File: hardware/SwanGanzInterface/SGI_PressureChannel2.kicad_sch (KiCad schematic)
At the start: 18 parts, among them J7 Conn_01x04_Pin, U12 INA122D, U13 OPA2350

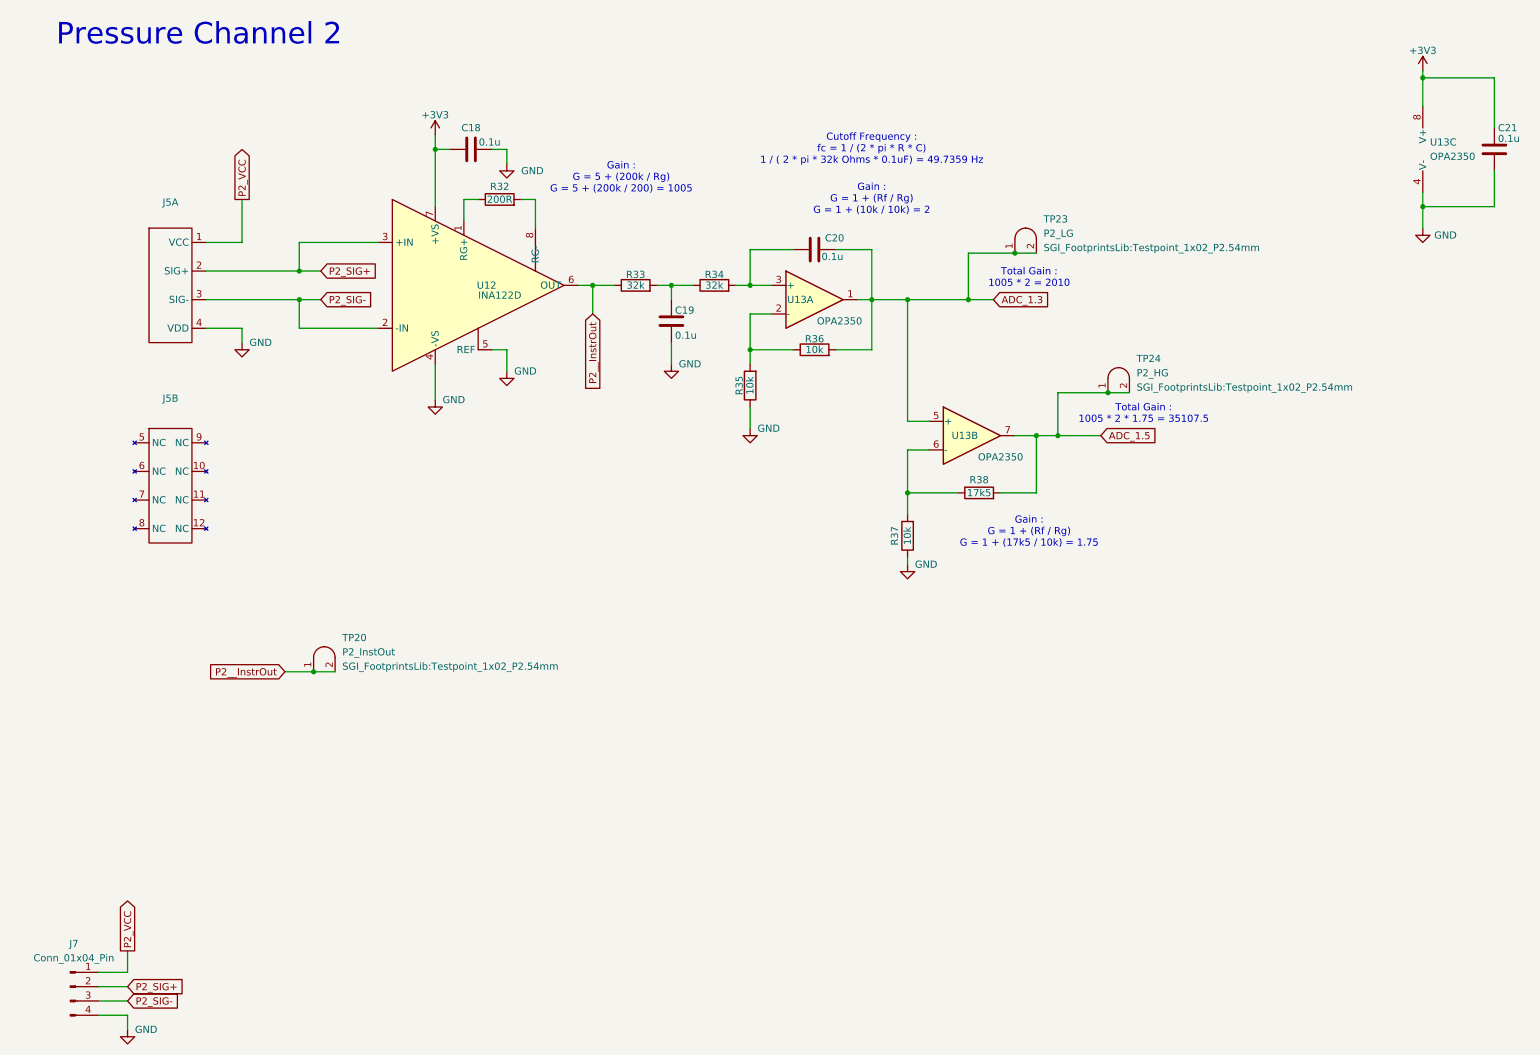
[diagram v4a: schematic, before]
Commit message: Reannotated symbols
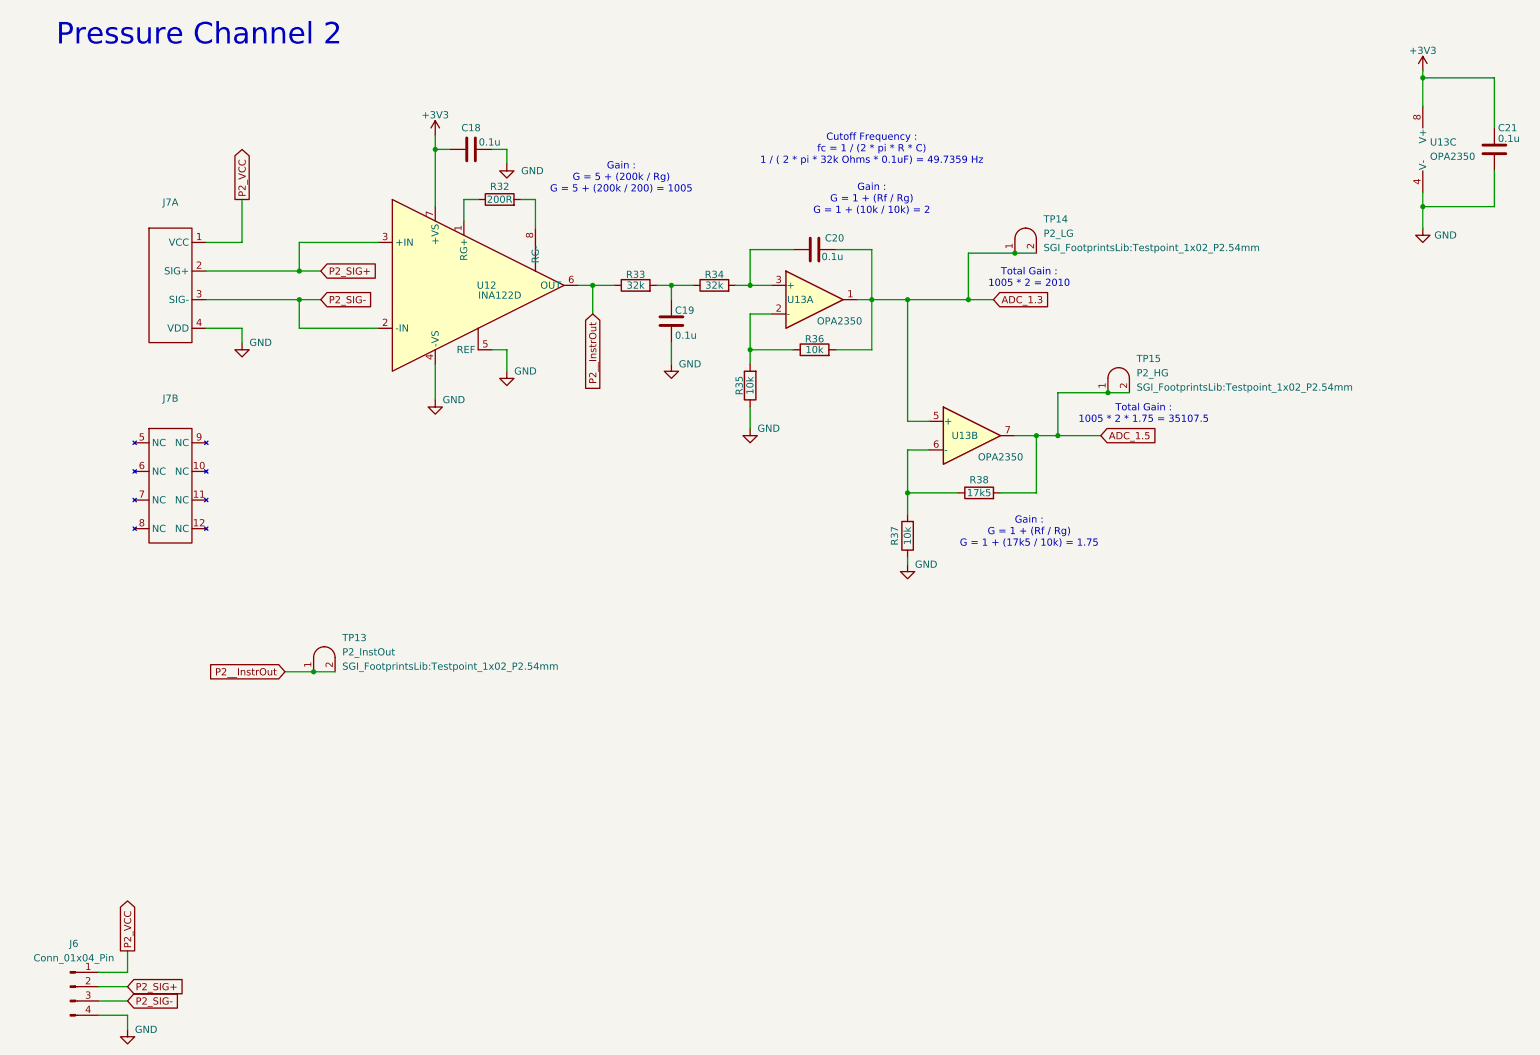
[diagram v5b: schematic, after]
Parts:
- renumbered J7 to J6, J5 to J7, TP20 to TP13, TP23 to TP14, TP24 to TP15
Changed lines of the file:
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@@
 		(on_board yes)
 		(dnp no)
-		(property "Reference" "#PWR070"
+		(property "Reference" "#PWR069"
 			(at 259.08 27.94 0)
 			(effects
@@
 			(project "SwanGanzInterface"
 				(path "/4e9a6e30-f660-472b-9696-bea1f34b4545/5b443651-3bea-4d19-bd25-a234ca65ad96"
-					(reference "#PWR070")
+					(reference "#PWR069")
 					(unit 1)
 				)
@@
 		(on_board yes)
 		(dnp no)
-		(property "Reference" "#PWR073"
+		(property "Reference" "#PWR060"
 			(at 29.21 200.66 0)
 			(effects
@@
 			(project "SwanGanzInterface"
 				(path "/4e9a6e30-f660-472b-9696-bea1f34b4545/5b443651-3bea-4d19-bd25-a234ca65ad96"
-					(reference "#PWR073")
+					(reference "#PWR060")
 					(unit 1)
 				)
@@
 		(dnp no)
 		(fields_autoplaced yes)
-		(property "Reference" "J7"
+		(property "Reference" "J6"
 			(at 19.685 179.07 0)
 			(effects
@@
 			(project "SwanGanzInterface"
 				(path "/4e9a6e30-f660-472b-9696-bea1f34b4545/5b443651-3bea-4d19-bd25-a234ca65ad96"
-					(reference "J7")
+					(reference "J6")
 					(unit 1)
 				)
@@
 		(dnp no)
 		(fields_autoplaced yes)
-		(property "Reference" "J5"
+		(property "Reference" "J7"
 			(at 36.83 47.498 0)
 			(effects
@@
 			(project "SwanGanzInterface"
 				(path "/4e9a6e30-f660-472b-9696-bea1f34b4545/5b443651-3bea-4d19-bd25-a234ca65ad96"
-					(reference "J5")
+					(reference "J7")
 					(unit 1)
 				)
@@
 		(on_board yes)
 		(dnp no)
-		(property "Reference" "#PWR069"
+		(property "Reference" "#PWR068"
 			(at 167.64 118.11 0)
 			(effects
@@
 			(project "SwanGanzInterface"
 				(path "/4e9a6e30-f660-472b-9696-bea1f34b4545/5b443651-3bea-4d19-bd25-a234ca65ad96"
-					(reference "#PWR069")
+					(reference "#PWR068")
 					(unit 1)
 				)
@@
 		(on_board yes)
 		(dnp no)
-		(property "Reference" "#PWR067"
+		(property "Reference" "#PWR066"
 			(at 125.73 82.55 0)
 			(effects
@@
 			(project "SwanGanzInterface"
 				(path "/4e9a6e30-f660-472b-9696-bea1f34b4545/5b443651-3bea-4d19-bd25-a234ca65ad96"
-					(reference "#PWR067")
+					(reference "#PWR066")
 					(unit 1)
 				)
@@
 		(on_board yes)
 		(dnp no)
-		(property "Reference" "#PWR068"
+		(property "Reference" "#PWR067"
 			(at 139.7 93.98 0)
 			(effects
@@
 			(project "SwanGanzInterface"
 				(path "/4e9a6e30-f660-472b-9696-bea1f34b4545/5b443651-3bea-4d19-bd25-a234ca65ad96"
-					(reference "#PWR068")
+					(reference "#PWR067")
 					(unit 1)
 				)
@@
 		(dnp no)
 		(fields_autoplaced yes)
-		(property "Reference" "TP23"
+		(property "Reference" "TP14"
 			(at 191.77 50.4823 0)
 			(effects
@@
 			(project "SwanGanzInterface"
 				(path "/4e9a6e30-f660-472b-9696-bea1f34b4545/5b443651-3bea-4d19-bd25-a234ca65ad96"
-					(reference "TP23")
+					(reference "TP14")
 					(unit 1)
 				)
@@
 		(dnp no)
 		(fields_autoplaced yes)
-		(property "Reference" "TP20"
+		(property "Reference" "TP13"
 			(at 67.31 124.7773 0)
 			(effects
@@
 			(project "SwanGanzInterface"
 				(path "/4e9a6e30-f660-472b-9696-bea1f34b4545/5b443651-3bea-4d19-bd25-a234ca65ad96"
-					(reference "TP20")
+					(reference "TP13")
 					(unit 1)
 				)
@@
 		(dnp no)
 		(fields_autoplaced yes)
-		(property "Reference" "J5"
+		(property "Reference" "J7"
 			(at 36.83 82.296 0)
 			(effects
@@
 			(project "SwanGanzInterface"
 				(path "/4e9a6e30-f660-472b-9696-bea1f34b4545/5b443651-3bea-4d19-bd25-a234ca65ad96"
-					(reference "J5")
+					(reference "J7")
 					(unit 2)
 				)
@@
 		(on_board yes)
 		(dnp no)
-		(property "Reference" "#PWR064"
+		(property "Reference" "#PWR063"
 			(at 83.82 88.9 0)
 			(effects
@@
 			(project "SwanGanzInterface"
 				(path "/4e9a6e30-f660-472b-9696-bea1f34b4545/5b443651-3bea-4d19-bd25-a234ca65ad96"
-					(reference "#PWR064")
+					(reference "#PWR063")
 					(unit 1)
 				)
@@
 		(dnp no)
 		(fields_autoplaced yes)
-		(property "Reference" "TP24"
+		(property "Reference" "TP15"
 			(at 208.28 75.2473 0)
 			(effects
@@
 			(project "SwanGanzInterface"
 				(path "/4e9a6e30-f660-472b-9696-bea1f34b4545/5b443651-3bea-4d19-bd25-a234ca65ad96"
-					(reference "TP24")
+					(reference "TP15")
 					(unit 1)
 				)
@@
 		(dnp no)
 		(fields_autoplaced yes)
-		(property "Reference" "#PWR071"
+		(property "Reference" "#PWR070"
 			(at 259.08 58.42 0)
 			(effects
@@
 			(project "SwanGanzInterface"
 				(path "/4e9a6e30-f660-472b-9696-bea1f34b4545/5b443651-3bea-4d19-bd25-a234ca65ad96"
-					(reference "#PWR071")
+					(reference "#PWR070")
 					(unit 1)
 				)
@@
 		(on_board yes)
 		(dnp no)
-		(property "Reference" "#PWR063"
+		(property "Reference" "#PWR062"
 			(at 83.82 39.37 0)
 			(effects
@@
 			(project "SwanGanzInterface"
 				(path "/4e9a6e30-f660-472b-9696-bea1f34b4545/5b443651-3bea-4d19-bd25-a234ca65ad96"
-					(reference "#PWR063")
+					(reference "#PWR062")
 					(unit 1)
 				)
@@
 		(dnp no)
 		(fields_autoplaced yes)
-		(property "Reference" "#PWR065"
+		(property "Reference" "#PWR064"
 			(at 96.52 46.99 0)
 			(effects
@@
 			(project "SwanGanzInterface"
 				(path "/4e9a6e30-f660-472b-9696-bea1f34b4545/5b443651-3bea-4d19-bd25-a234ca65ad96"
-					(reference "#PWR065")
+					(reference "#PWR064")
 					(unit 1)
 				)
@@
 		(on_board yes)
 		(dnp no)
-		(property "Reference" "#PWR062"
+		(property "Reference" "#PWR061"
 			(at 49.53 78.74 0)
 			(effects
@@
 			(project "SwanGanzInterface"
 				(path "/4e9a6e30-f660-472b-9696-bea1f34b4545/5b443651-3bea-4d19-bd25-a234ca65ad96"
-					(reference "#PWR062")
+					(reference "#PWR061")
 					(unit 1)
 				)
@@
 		(on_board yes)
 		(dnp no)
-		(property "Reference" "#PWR066"
+		(property "Reference" "#PWR065"
 			(at 96.52 83.82 0)
 			(effects
@@
 			(project "SwanGanzInterface"
 				(path "/4e9a6e30-f660-472b-9696-bea1f34b4545/5b443651-3bea-4d19-bd25-a234ca65ad96"
-					(reference "#PWR066")
-					(unit 1)
-				)
+					(reference "#PWR065")
+					(unit 1)
+				)

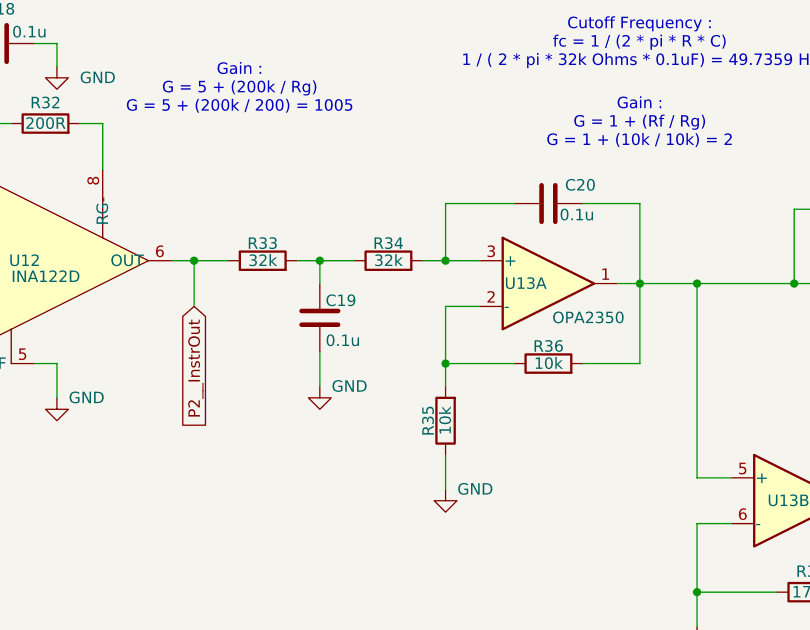
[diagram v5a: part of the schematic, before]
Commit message: Fixed butterworth filters
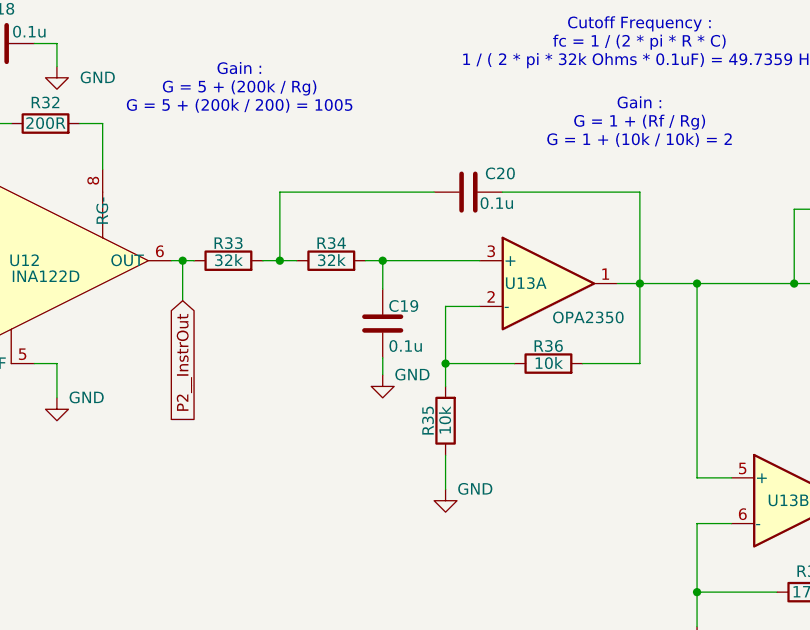
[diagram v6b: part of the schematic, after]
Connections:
- net at R33.2, R34.1: now also C20.1; no longer C19.1
- net at R34.2, U13.3 (+): now also C19.1; no longer C20.1
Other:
- moved on the sheet: C19, C20, R33, R34

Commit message: Implemented Jack's new pressure footprint and added teardrop - new production file
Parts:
- J7: footprint SGI_FootprintsLib:Pressure_Connector -> SGI_FootprintsLib:Pressure_Connector_1.1
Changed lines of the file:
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@@
 			)
 		)
-		(property "Footprint" "SGI_FootprintsLib:Pressure_Connector"
+		(property "Footprint" "SGI_FootprintsLib:Pressure_Connector_1.1"
 			(at 36.83 62.23 0)
 			(effects
@@
 			)
 		)
-		(property "Footprint" "SGI_FootprintsLib:Pressure_Connector"
+		(property "Footprint" "SGI_FootprintsLib:Pressure_Connector_1.1"
 			(at 36.83 97.79 0)
 			(effects

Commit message: Driver Power
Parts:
- renumbered R32 to R31, R33 to R32, R34 to R33, R35 to R34, R36 to R35, R37 to R36, R38 to R37
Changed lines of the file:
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@@
 		(on_board yes)
 		(dnp no)
-		(property "Reference" "#PWR069"
+		(property "Reference" "#PWR068"
 			(at 259.08 27.94 0)
 			(effects
@@
 			(project "SwanGanzInterface"
 				(path "/4e9a6e30-f660-472b-9696-bea1f34b4545/5b443651-3bea-4d19-bd25-a234ca65ad96"
-					(reference "#PWR069")
+					(reference "#PWR068")
 					(unit 1)
 				)
@@
 		(on_board yes)
 		(dnp no)
-		(property "Reference" "#PWR060"
+		(property "Reference" "#PWR059"
 			(at 29.21 200.66 0)
 			(effects
@@
 			(project "SwanGanzInterface"
 				(path "/4e9a6e30-f660-472b-9696-bea1f34b4545/5b443651-3bea-4d19-bd25-a234ca65ad96"
-					(reference "#PWR060")
+					(reference "#PWR059")
 					(unit 1)
 				)
@@
 		(on_board yes)
 		(dnp no)
-		(property "Reference" "#PWR068"
+		(property "Reference" "#PWR067"
 			(at 167.64 118.11 0)
 			(effects
@@
 			(project "SwanGanzInterface"
 				(path "/4e9a6e30-f660-472b-9696-bea1f34b4545/5b443651-3bea-4d19-bd25-a234ca65ad96"
-					(reference "#PWR068")
+					(reference "#PWR067")
 					(unit 1)
 				)
@@
 		(on_board yes)
 		(dnp no)
-		(property "Reference" "R36"
+		(property "Reference" "R35"
 			(at 151.13 71.755 90)
 			(effects
@@
 			(project "SwanGanzInterface"
 				(path "/4e9a6e30-f660-472b-9696-bea1f34b4545/5b443651-3bea-4d19-bd25-a234ca65ad96"
-					(reference "R36")
+					(reference "R35")
 					(unit 1)
 				)
@@
 		(on_board yes)
 		(dnp no)
-		(property "Reference" "R33"
+		(property "Reference" "R32"
 			(at 115.57 60.325 90)
 			(effects
@@
 			(project "SwanGanzInterface"
 				(path "/4e9a6e30-f660-472b-9696-bea1f34b4545/5b443651-3bea-4d19-bd25-a234ca65ad96"
-					(reference "R33")
+					(reference "R32")
 					(unit 1)
 				)
@@
 		(on_board yes)
 		(dnp no)
-		(property "Reference" "#PWR066"
+		(property "Reference" "#PWR065"
 			(at 132.715 81.28 0)
 			(effects
@@
 			(project "SwanGanzInterface"
 				(path "/4e9a6e30-f660-472b-9696-bea1f34b4545/5b443651-3bea-4d19-bd25-a234ca65ad96"
-					(reference "#PWR066")
+					(reference "#PWR065")
 					(unit 1)
 				)
@@
 		(on_board yes)
 		(dnp no)
-		(property "Reference" "#PWR067"
+		(property "Reference" "#PWR066"
 			(at 139.7 93.98 0)
 			(effects
@@
 			(project "SwanGanzInterface"
 				(path "/4e9a6e30-f660-472b-9696-bea1f34b4545/5b443651-3bea-4d19-bd25-a234ca65ad96"
-					(reference "#PWR067")
+					(reference "#PWR066")
 					(unit 1)
 				)
@@
 		(on_board yes)
 		(dnp no)
-		(property "Reference" "R35"
+		(property "Reference" "R34"
 			(at 137.795 80.01 90)
 			(effects
@@
 			(project "SwanGanzInterface"
 				(path "/4e9a6e30-f660-472b-9696-bea1f34b4545/5b443651-3bea-4d19-bd25-a234ca65ad96"
-					(reference "R35")
+					(reference "R34")
 					(unit 1)
 				)
@@
 		(on_board yes)
 		(dnp no)
-		(property "Reference" "R32"
+		(property "Reference" "R31"
 			(at 95.25 44.704 90)
 			(effects
@@
 			(project "SwanGanzInterface"
 				(path "/4e9a6e30-f660-472b-9696-bea1f34b4545/5b443651-3bea-4d19-bd25-a234ca65ad96"
-					(reference "R32")
+					(reference "R31")
 					(unit 1)
 				)
@@
 		(on_board yes)
 		(dnp no)
-		(property "Reference" "#PWR063"
+		(property "Reference" "#PWR062"
 			(at 83.82 88.9 0)
 			(effects
@@
 			(project "SwanGanzInterface"
 				(path "/4e9a6e30-f660-472b-9696-bea1f34b4545/5b443651-3bea-4d19-bd25-a234ca65ad96"
-					(reference "#PWR063")
+					(reference "#PWR062")
 					(unit 1)
 				)
@@
 		(on_board yes)
 		(dnp no)
-		(property "Reference" "R34"
+		(property "Reference" "R33"
 			(at 127 60.325 90)
 			(effects
@@
 			(project "SwanGanzInterface"
 				(path "/4e9a6e30-f660-472b-9696-bea1f34b4545/5b443651-3bea-4d19-bd25-a234ca65ad96"
-					(reference "R34")
+					(reference "R33")
 					(unit 1)
 				)
@@
 		(on_board yes)
 		(dnp no)
-		(property "Reference" "R38"
+		(property "Reference" "R37"
 			(at 180.34 96.774 90)
 			(effects
@@
 			(project "SwanGanzInterface"
 				(path "/4e9a6e30-f660-472b-9696-bea1f34b4545/5b443651-3bea-4d19-bd25-a234ca65ad96"
-					(reference "R38")
+					(reference "R37")
 					(unit 1)
 				)
@@
 		(dnp no)
 		(fields_autoplaced yes)
-		(property "Reference" "#PWR070"
+		(property "Reference" "#PWR069"
 			(at 259.08 58.42 0)
 			(effects
@@
 			(project "SwanGanzInterface"
 				(path "/4e9a6e30-f660-472b-9696-bea1f34b4545/5b443651-3bea-4d19-bd25-a234ca65ad96"
-					(reference "#PWR070")
+					(reference "#PWR069")
 					(unit 1)
 				)
@@
 		(on_board yes)
 		(dnp no)
-		(property "Reference" "#PWR062"
+		(property "Reference" "#PWR061"
 			(at 83.82 39.37 0)
 			(effects
@@
 			(project "SwanGanzInterface"
 				(path "/4e9a6e30-f660-472b-9696-bea1f34b4545/5b443651-3bea-4d19-bd25-a234ca65ad96"
-					(reference "#PWR062")
+					(reference "#PWR061")
 					(unit 1)
 				)
@@
 		(dnp no)
 		(fields_autoplaced yes)
-		(property "Reference" "#PWR064"
+		(property "Reference" "#PWR063"
 			(at 96.52 46.99 0)
 			(effects
@@
 			(project "SwanGanzInterface"
 				(path "/4e9a6e30-f660-472b-9696-bea1f34b4545/5b443651-3bea-4d19-bd25-a234ca65ad96"
-					(reference "#PWR064")
+					(reference "#PWR063")
 					(unit 1)
 				)
@@
 		(on_board yes)
 		(dnp no)
-		(property "Reference" "#PWR061"
+		(property "Reference" "#PWR060"
 			(at 49.53 78.74 0)
 			(effects
@@
 			(project "SwanGanzInterface"
 				(path "/4e9a6e30-f660-472b-9696-bea1f34b4545/5b443651-3bea-4d19-bd25-a234ca65ad96"
-					(reference "#PWR061")
+					(reference "#PWR060")
 					(unit 1)
 				)
@@
 		(on_board yes)
 		(dnp no)
-		(property "Reference" "#PWR065"
+		(property "Reference" "#PWR064"
 			(at 96.52 83.82 0)
 			(effects
@@
 			(project "SwanGanzInterface"
 				(path "/4e9a6e30-f660-472b-9696-bea1f34b4545/5b443651-3bea-4d19-bd25-a234ca65ad96"
-					(reference "#PWR065")
+					(reference "#PWR064")
 					(unit 1)
 				)
@@
 		(on_board yes)
 		(dnp no)
-		(property "Reference" "R37"
+		(property "Reference" "R36"
 			(at 165.354 106.68 90)
 			(effects
@@
 			(project "SwanGanzInterface"
 				(path "/4e9a6e30-f660-472b-9696-bea1f34b4545/5b443651-3bea-4d19-bd25-a234ca65ad96"
-					(reference "R37")
-					(unit 1)
-				)
+					(reference "R36")
+					(unit 1)
+				)
